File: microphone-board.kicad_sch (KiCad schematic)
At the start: 13 parts, among them J1 Conn_FFC_Molex_5019510550

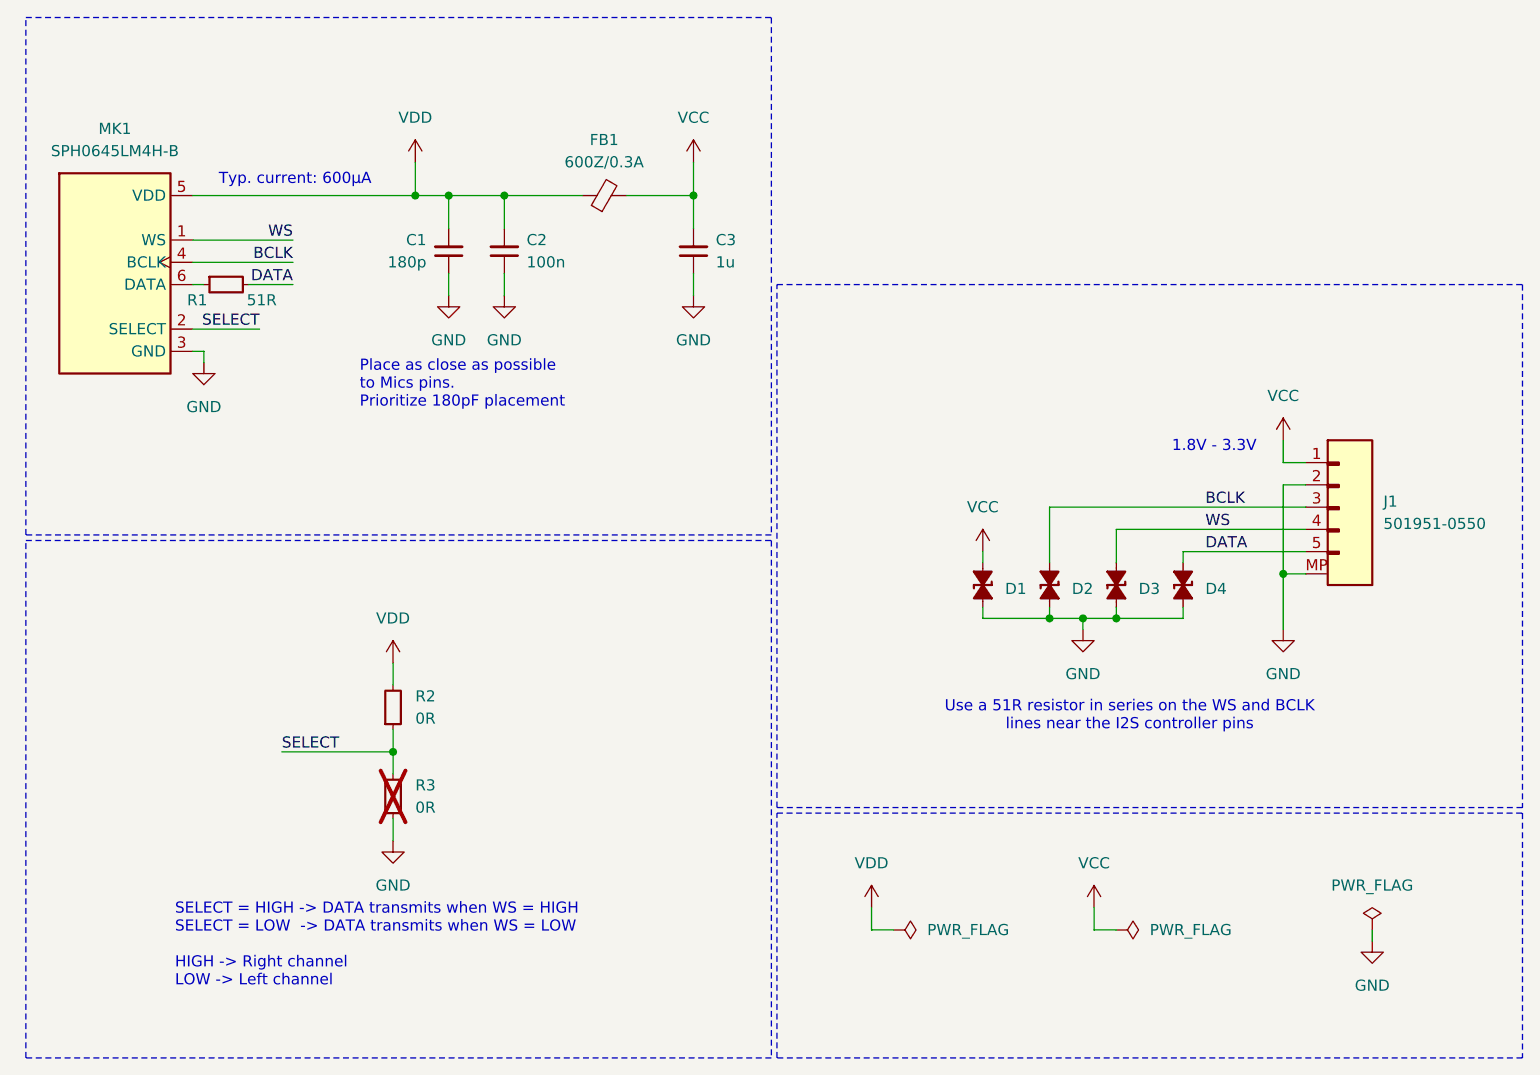
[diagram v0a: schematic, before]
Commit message: [#72278] Replace the microphone with MK_SPH0644LM4H-1 (PDM)
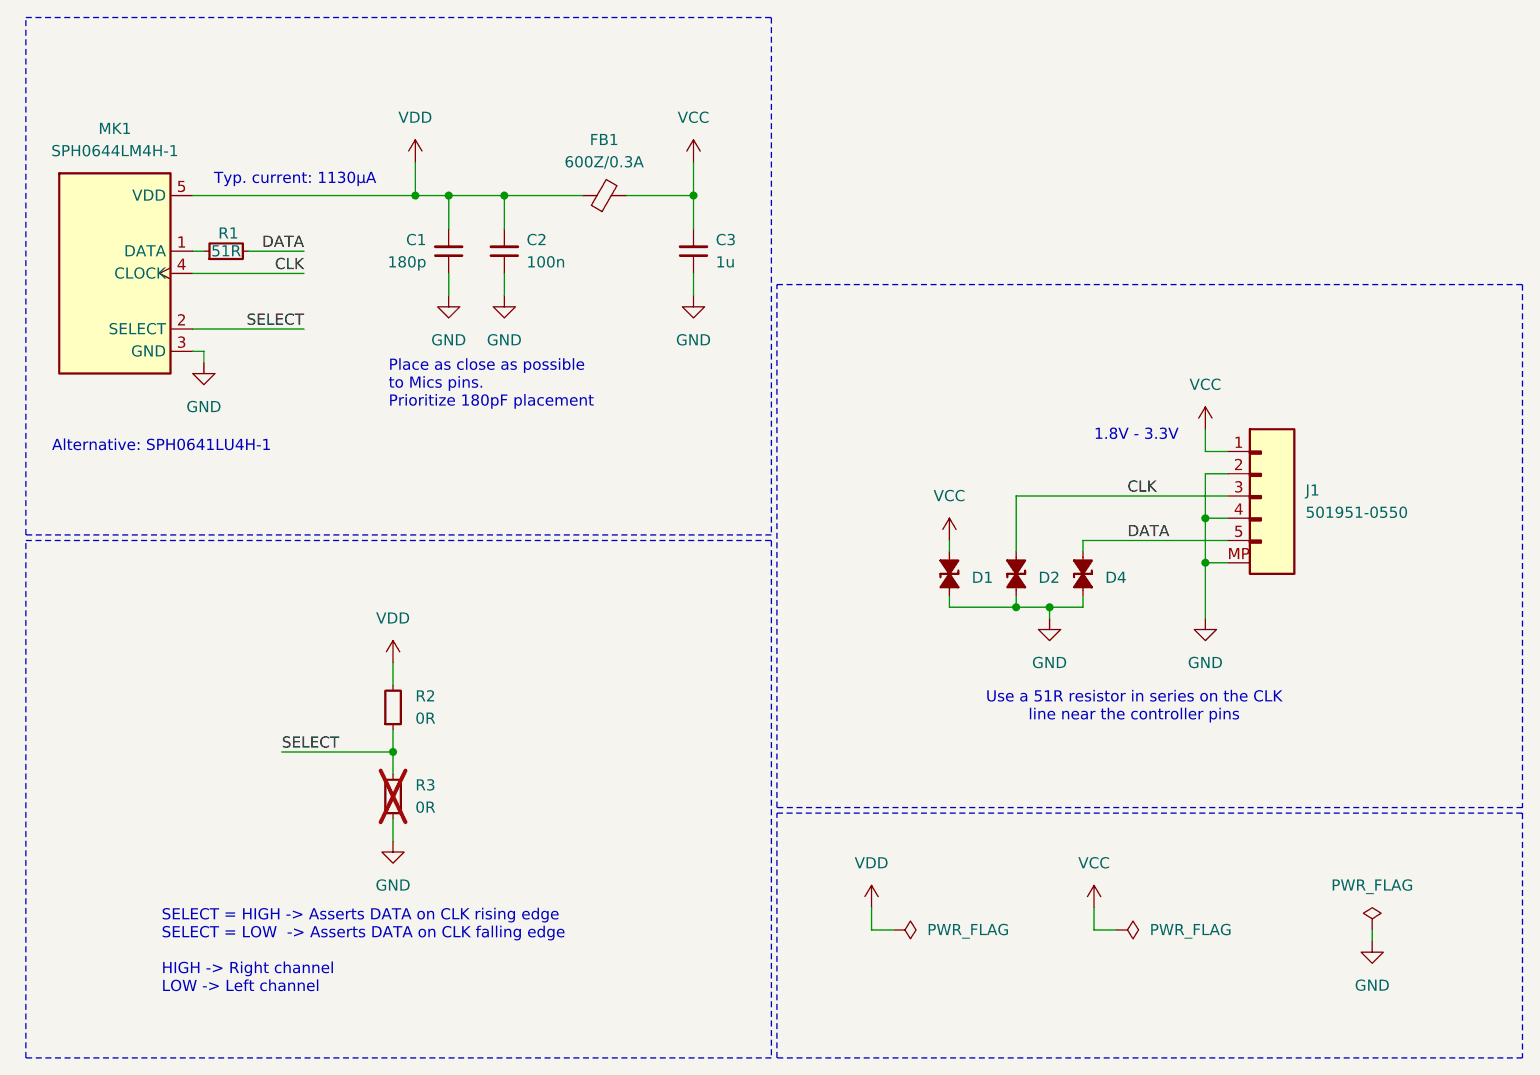
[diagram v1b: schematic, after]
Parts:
- removed D3: TPD1E0B04_XDFN-2, antmicro-footprints:XDFN-2_1x0.60mm, symbol antmicroTVSDiodes:TPD1E0B04_XDFN-2
- removed MK1: MK_SPH0645LM4H-B, antmicro-footprints:MK_SPH0645LM4H-B, symbol antmicroMicrophones:MK_SPH0645LM4H-B
- added MK1: MK_SPH0644LM4H-1, antmicro-footprints:MK_SPH0644LM4H-1, symbol antmicroMicrophones:MK_SPH0644LM4H-1
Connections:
- net WS is gone; now on net GND: J1.4
- net GND: now also MK1.3 (GND)
- net SELECT: now also MK1.2 (SELECT)
- net VDD: now also MK1.5 (VDD)
- net at R1.1: now also MK1.1 (DATA)
- net BCLK renamed CLK
- net CLK: now also MK1.4 (CLOCK)
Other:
- note added: "Alternative: SPH0641LU4H-1"
- note added: "SELECT = HIGH -> Asserts DATA on CLK rising edge SELECT = LOW -> Asserts DATA on CLK falling edge HIGH -> Right channel LOW -> Left channel"
- note added: "Typ. current: 1130µA"
- note added: "Use a 51R resistor in series on the CLK line near the controller pins"
- note removed: "SELECT = HIGH -> DATA transmits when WS = HIGH SELECT = LOW -> DATA transmits when WS = LOW HIGH -> Right channel LOW -> Left channel"
- note removed: "Typ. current: 600µA"
- note removed: "Use a 51R resistor in series on the WS and BCLK lines near the I2S controller pins"
- moved on the sheet: D1, D2, D4, J1, R1

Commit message: [#72278] Set TVS MPN to visible
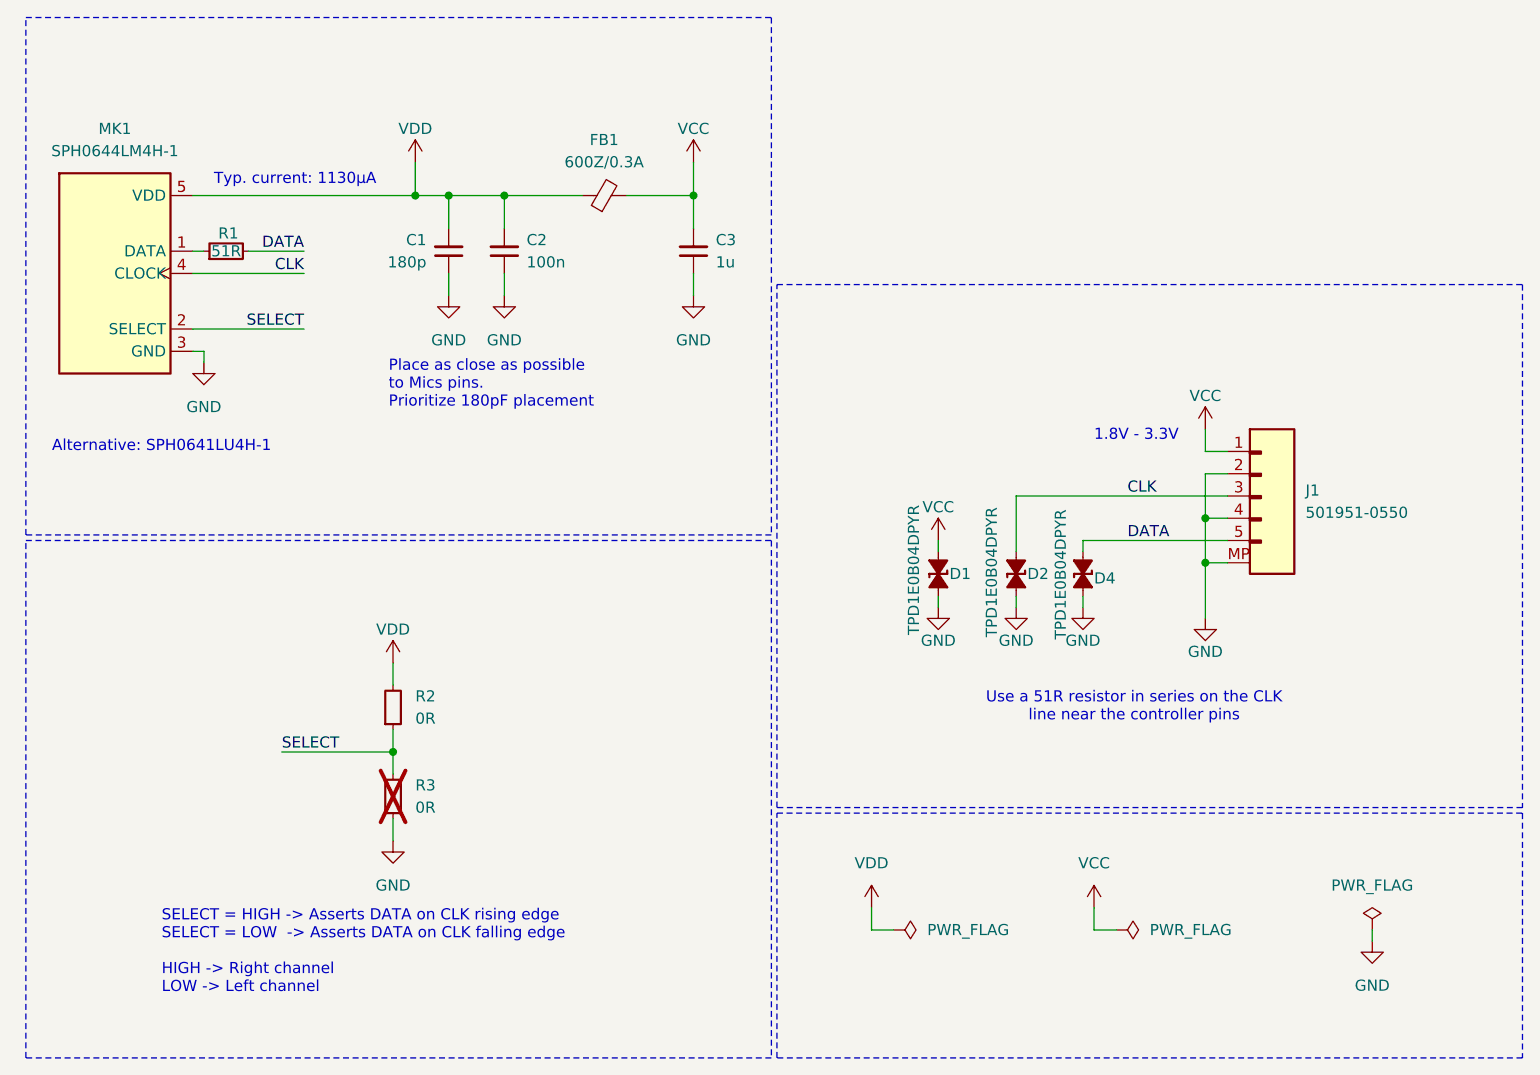
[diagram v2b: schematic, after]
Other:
- title: Microphone board -> Microphone Board
- moved on the sheet: D1
